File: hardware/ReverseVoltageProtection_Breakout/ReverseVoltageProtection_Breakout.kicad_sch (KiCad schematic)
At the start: 5 parts, among them Q1 Q_PMOS_DGS

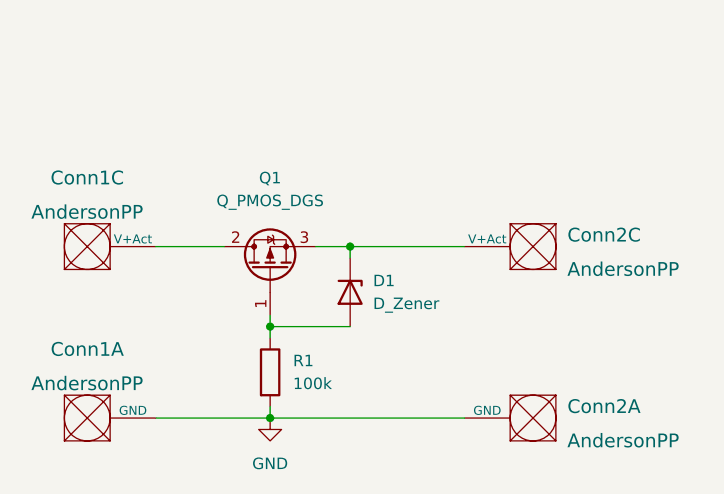
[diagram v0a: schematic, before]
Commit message: made 12V version
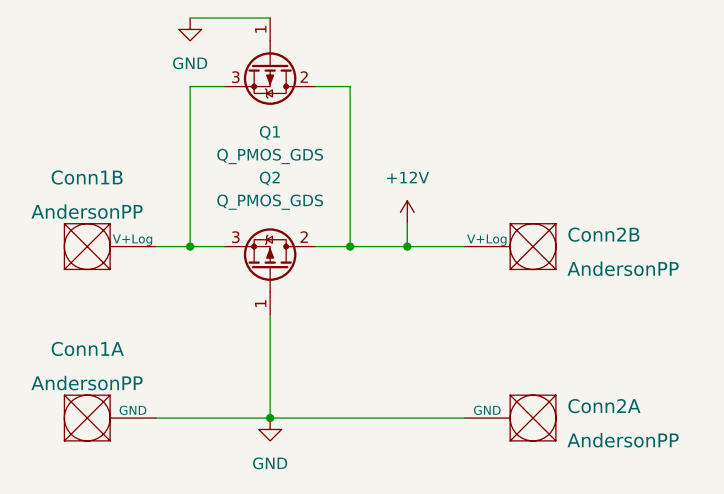
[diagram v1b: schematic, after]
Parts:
- removed D1: D_Zener, Package_TO_SOT_SMD:SOT-23-3, symbol Device:D_Zener
- removed R1: 100k, Resistor_SMD:R_0603_1608Metric_Pad0.98x0.95mm_HandSolder, symbol Device:R
- added Q2: Q_PMOS_GDS, Package_TO_SOT_SMD:TO-252-3_TabPin2, symbol Device:Q_PMOS_GDS
- Conn1, Conn2: footprint MRDT_Connectors:Square_Anderson_2_H_Side_By_Side -> MRDT_Connectors:Square_Anderson_2_V_Side_By_Side
- Q1: value Q_PMOS_DGS -> Q_PMOS_GDS
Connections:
- net GND: now also Q1.1 (G), Q2.1 (G)
- net at Q1.3 (S): now also Conn1.2 (V+Log), Q2.3 (S); no longer Conn2.3 (V+Act)
- net +12V: now reaches Q1.2 (D)
- net +12V: now also Conn2.2 (V+Log), Q2.2 (D); no longer Conn1.3 (V+Act)
